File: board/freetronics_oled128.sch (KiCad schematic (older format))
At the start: 38 parts, among them IC1 TPS61040, P1 M02X05, P2 MICROSD, P3 M02X02, P4 M02X02, Q1 2N7002, SW1 SW_PUSHBUTTON, SW2 SW_PUSHBUTTON, U1 MC74VHCT50A

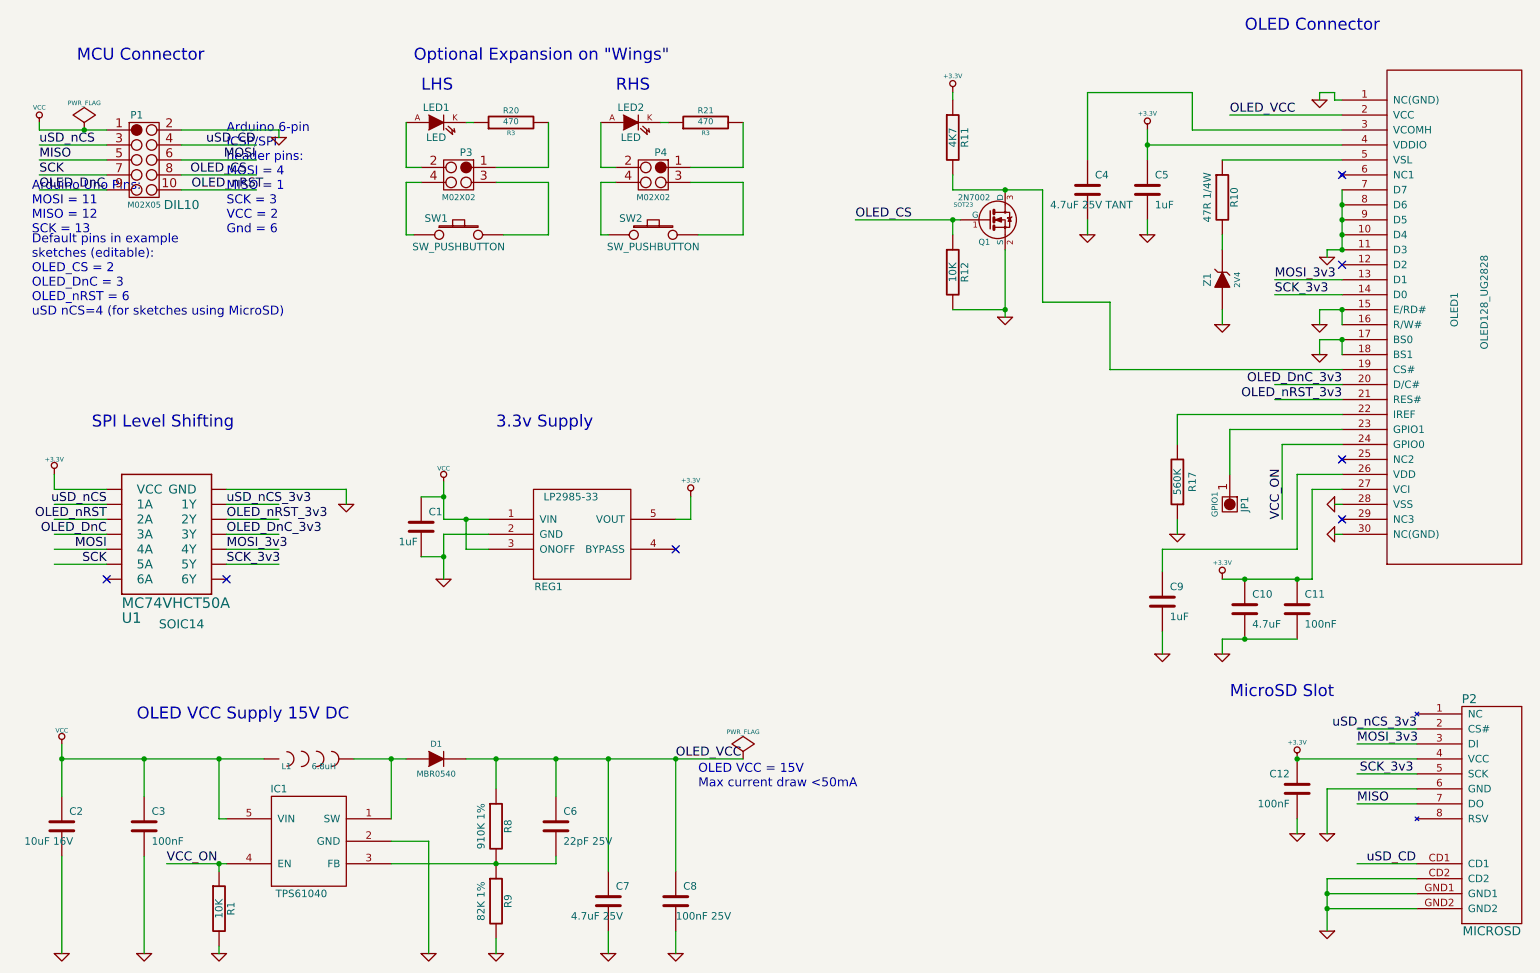
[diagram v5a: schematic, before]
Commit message: Remove inverting OLED_CS transistor Q1, use remaining buffer channel instead
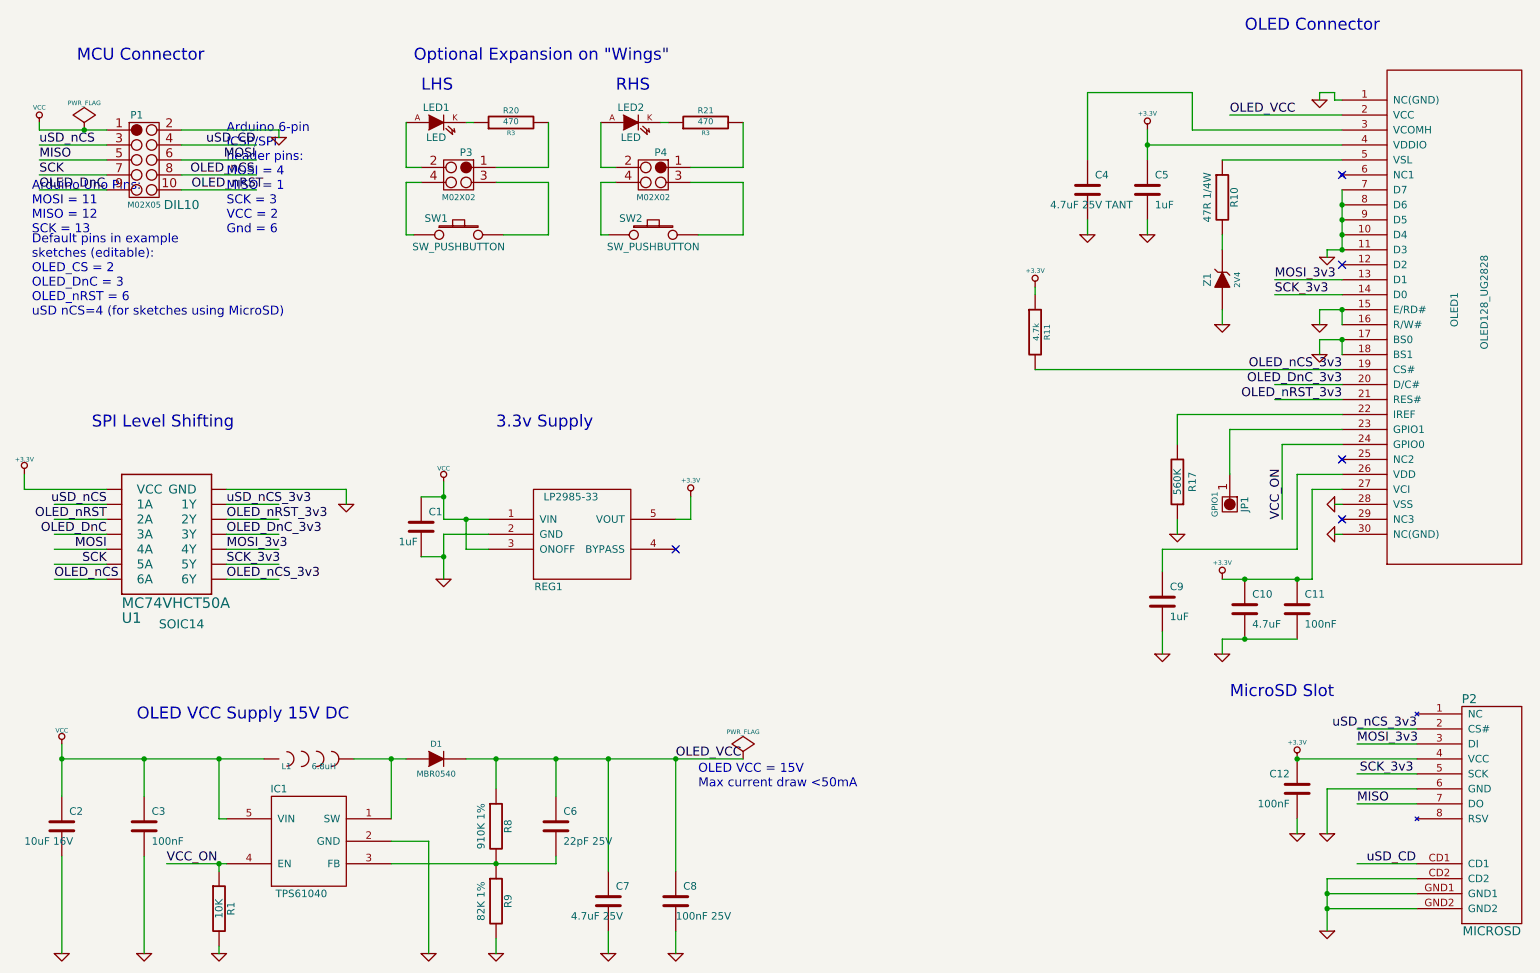
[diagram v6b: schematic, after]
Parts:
- removed Q1: 2N7002, SOT23, symbol 2N7002
- removed R12: 10K, 0603, symbol R
- R11: value 4K7 -> 4.7k; footprint 0603 -> ~
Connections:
- net labels added: OLED_nCS, OLED_nCS_3v3
- net labels removed: OLED_CS
- wire segments 154 -> 147
- no-connect marks 7 -> 5
